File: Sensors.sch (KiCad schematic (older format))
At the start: 42 parts, among them CN4 CONN_HEADER_SMD_4POS_2MM, U10 MPXV4006GP, U11 MPXV4006DP, U12 TLV2333IDR, U16 SFM3020, U17 MPXV4006GP, U7 LPS25HB

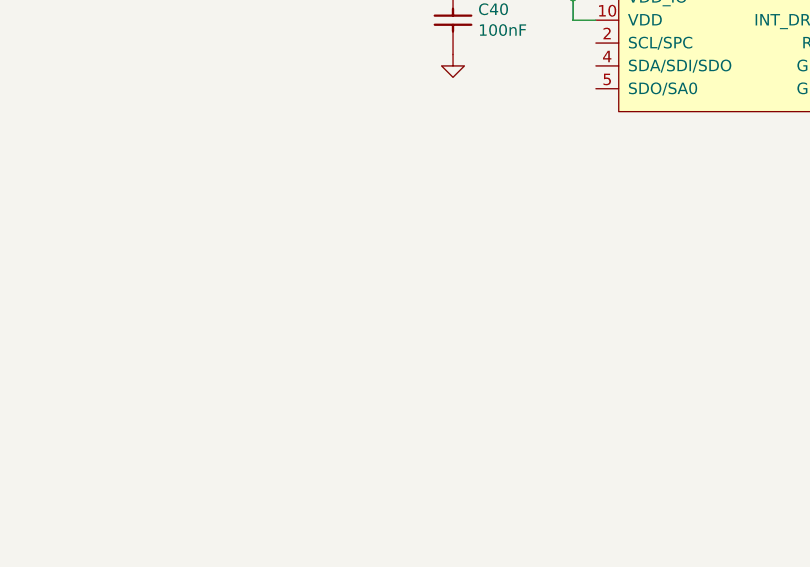
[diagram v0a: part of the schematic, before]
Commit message: MOLEX connector added for SFM3019 external flow sensor
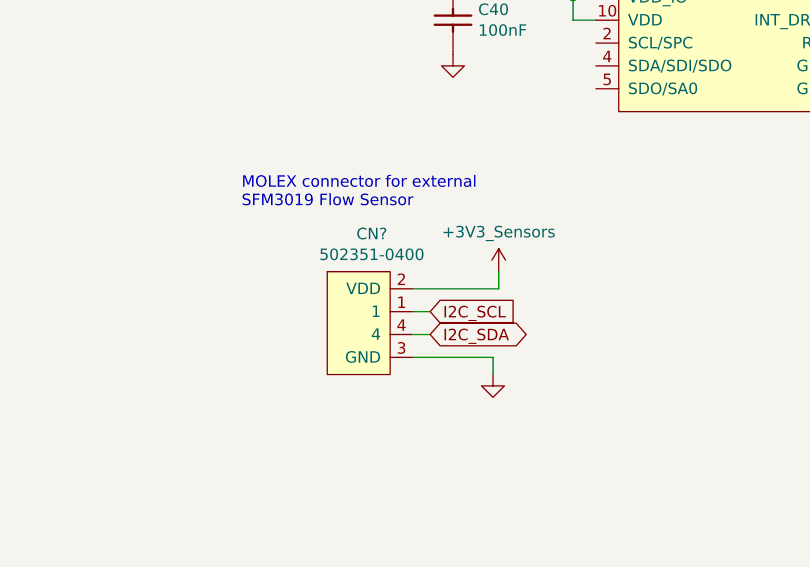
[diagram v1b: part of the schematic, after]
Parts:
- added CN?: 502351-0400, symbol OpenVent:502351-0400
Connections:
- net labels added: +3V3_Sensors, I2C_SCL, I2C_SDA
- wire segments 129 -> 135
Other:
- note added: "MOLEX connector for external\nSFM3019 Flow Sensor"
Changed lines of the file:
@@
 	9625 4775 9625 4675
 Connection ~ 9625 4775
+$Comp
+L OpenVent:502351-0400 CN?
+U 1 1 6027899F
+P 7425 5525
+F 0 "CN?" H 7470 5540 50  0000 C CNN
+F 1 "502351-0400" H 7470 5449 50  0000 C CNN
+F 2 "" H 7425 5525 50  0001 C CNN
+F 3 "" H 7425 5525 50  0001 C CNN
+	1    7425 5525
+	1    0    0    -1
+$EndComp
+$Comp
+L OpenVent:+3V3_Sensors #PWR?
+U 1 1 6027FA4F
+P 8025 5675
+F 0 "#PWR?" H 8025 5525 50  0001 C CNN
+F 1 "+3V3_Sensors" H 8025 5848 50  0000 C CNN
+F 2 "" H 8025 5675 50  0001 C CNN
+F 3 "" H 8025 5675 50  0001 C CNN
+	1    8025 5675
+	1    0    0    -1
+$EndComp
+$Comp
+L OpenVent:GND #PWR?
+U 1 1 6028A518
+P 8000 6125
+F 0 "#PWR?" H 8000 5875 50  0001 C CNN
+F 1 "GND" H 8000 5975 50  0001 C CNN
+F 2 "" H 8000 6125 50  0001 C CNN
+F 3 "" H 8000 6125 50  0001 C CNN
+	1    8000 6125
+	1    0    0    -1
+$EndComp
+Wire Wire Line
+	7650 6050 8000 6050
+Wire Wire Line
+	8000 6050 8000 6125
+Wire Wire Line
+	7650 5750 8025 5750
+Wire Wire Line
+	8025 5750 8025 5675
+Text GLabel 7725 5850 2    50   Input ~ 0
+I2C_SCL
+Text GLabel 7725 5950 2    50   BiDi ~ 0
+I2C_SDA
+Wire Wire Line
+	7650 5850 7725 5850
+Wire Wire Line
+	7650 5950 7725 5950
+Text Notes 6900 5400 0    50   ~ 0
+MOLEX connector for external\nSFM3019 Flow Sensor
 $EndSCHEMATC

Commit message: Removed U16 SFM3020 sensor, changed symbol for CN4 (the off-board connector)
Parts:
- removed C67: 1nF_0603_Ceramic_Capacitor,_10%,_X7R,_25V, symbol OpenVent:1nF_0603_Ceramic_Capacitor,_10%,_X7R,_25V
- removed CN4: CONN_HEADER_SMD_4POS_2MM, symbol OpenVent:CONN_HEADER_SMD_4POS_2MM
- removed R31: 100K_0603_Chip_Resistor,_1%,_0.1W, Resistor_SMD:R_0603_1608Metric, symbol OpenVent:100K_0603_Chip_Resistor,_1%,_0.1W
- removed R34: 200k_0603_Chip_Resistor,_0.1%,_0.1W, Resistor_SMD:R_0603_1608Metric, symbol OpenVent:200k_0603_Chip_Resistor,_0.1%,_0.1W
- removed U16: SFM3020, symbol OpenVent:SFM3020
- added CN4: 502351-0400, symbol OpenVent:502351-0400
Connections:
- net labels removed: SENSIRON-FLOW-SENSOR
- wire segments 135 -> 126
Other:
- note added: "Molex connector for external\nSFM3020 flow sensor"
- note added: "NB Molex connector is into external connector,\nshould same molex connector be used on the PCB,\nor deliberately use a different one so cable can't be\nplugged in wrong way around? LM 08/02/21"
- note removed: "Alternative Flow Sensor Connector"
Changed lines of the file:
@@
 $EndComp
 Text Notes 650  1550 0    60   ~ 0
-Alternative Flow Sensor Connector
+Molex connector for external\nSFM3020 flow sensor
 $Comp
 L OpenVent:GND #GND_031
@@
 	1    0    0    -1
 $EndComp
-NoConn ~ 1600 2150
+NoConn ~ 1475 1950
 Wire Wire Line
 	8550 2575 8550 3075
@@
 	2750 3650 2750 3750
 Wire Wire Line
-	2150 3650 2750 3650
-Wire Wire Line
-	1800 3650 2150 3650
-Wire Wire Line
 	3500 3350 3700 3350
 Wire Wire Line
-	1800 3350 2300 3350
-Wire Wire Line
-	2000 3050 2550 3050
-Wire Wire Line
-	1800 3050 2000 3050
-Wire Wire Line
 	3350 4350 3350 4450
 Wire Wire Line
@@
 Wire Wire Line
 	5800 2050 5700 2050
-Wire Wire Line
-	2300 1850 1600 1850
-Wire Wire Line
-	2300 3350 2300 1850
-Wire Wire Line
-	2150 1950 1600 1950
-Wire Wire Line
-	2150 3650 2150 1950
-Wire Wire Line
-	2000 2050 1600 2050
-Wire Wire Line
-	2000 3050 2000 2050
-Connection ~ 2000 3050
-Connection ~ 2150 3650
-Connection ~ 2300 3350
 Connection ~ 2550 2750
 Connection ~ 2750 4950
@@
 $EndComp
 $Comp
-L OpenVent:CONN_HEADER_SMD_4POS_2MM CN4
-U 1 1 5F8DD0A1
-P 1600 2150
-F 0 "CN4" H 2050 2600 50  0000 L BNN
-F 1 "CONN_HEADER_SMD_4POS_2MM" H 1600 2150 50  0001 C CNN
-F 2 "" H 1600 2150 50  0001 C CNN
-F 3 "" H 1600 2150 50  0001 C CNN
-F 4 "Molex" H 1600 2150 50  0001 C CNN "Mfr"
-F 5 "5600200420" H 1600 2150 50  0001 C CNN "Mfr_PN"
-	1    1600 2150
-	-1   0    0    -1
-$EndComp
-$Comp
 L OpenVent:10nF_0603_Ceramic_Capacitor,_10%,_50V,_X7R- C32
 U 1 1 5F8DD0A0
@@
 Wire Wire Line
 	1800 4650 2950 4650
-Wire Wire Line
-	2300 3350 2950 3350
 $Comp
 L OpenVent:TLV2333IDR U12
@@
 Connection ~ 2750 5750
 $Comp
-L OpenVent:+5V #5V_010
-U 1 1 5FFC79F0
-P 1250 7000
-F 0 "#5V_010" H 1250 7000 20  0001 C CNN
-F 1 "+5V" H 1250 7150 50  0000 C CNN
-F 2 "" H 1250 7000 70  0000 C CNN
-F 3 "" H 1250 7000 70  0000 C CNN
-	1    1250 7000
-	1    0    0    -1
-$EndComp
-Wire Wire Line
-	1250 7125 1250 7000
-$Comp
-L OpenVent:GND #GND_030
-U 1 1 5FFDC913
-P 1250 7375
-F 0 "#GND_030" H 1250 7375 20  0001 C CNN
-F 1 "GND" H 1250 7305 50  0001 C CNN
-F 2 "" H 1250 7375 70  0000 C CNN
-F 3 "" H 1250 7375 70  0000 C CNN
-	1    1250 7375
-	1    0    0    -1
-$EndComp
-Wire Wire Line
-	1250 7375 1250 7225
-Text GLabel 4475 7125 2    60   Output ~ 0
-SENSIRON-FLOW-SENSOR
-$Comp
-L OpenVent:1nF_0603_Ceramic_Capacitor,_10%,_X7R,_25V C67
-U 1 1 5FFEE081
-P 3050 7250
-F 0 "C67" V 3054 7260 50  0000 L CNN
-F 1 "1nF_0603_Ceramic_Capacitor,_10%,_X7R,_25V" H 2525 7475 50  0001 C CNN
-F 2 "" H 3050 7250 50  0001 C CNN
-F 3 "" H 3050 7250 50  0001 C CNN
-F 4 "1nF" V 3145 7260 50  0000 L CNN "Val"
-F 5 "25V" H 2825 6925 50  0001 C CNN "Voltage"
-F 6 "10%" H 3125 6850 50  0001 C CNN "Tolerance"
-	1    3050 7250
-	0    1    1    0
-$EndComp
-$Comp
-L OpenVent:200k_0603_Chip_Resistor,_0.1%,_0.1W R34
-U 1 1 5FFF309C
-P 4150 7500
-F 0 "R34" V 4300 7150 50  0000 L BNN
-F 1 "200k_0603_Chip_Resistor,_0.1%,_0.1W" V 4150 7350 50  0001 C CNN
-F 2 "Resistor_SMD:R_0603_1608Metric" H 4050 7360 50  0001 C CNN
-F 3 "" H 4050 7360 50  0001 C CNN
-F 4 "0.1%" V 4100 7200 50  0000 C CNN "Tolerance"
-F 5 "200k" V 4200 7200 50  0000 C CNN "Val"
-F 6 "0.1W" H 4150 7500 50  0001 C CNN "Watt"
-	1    4150 7500
-	0    -1   -1   0
-$EndComp
-$Comp
-L OpenVent:100K_0603_Chip_Resistor,_1%,_0.1W R31
-U 1 1 5FFF367C
-P 3800 7025
-F 0 "R31" H 3800 6975 50  0000 L BNN
-F 1 "100K_0603_Chip_Resistor,_1%,_0.1W" H 3800 6775 50  0001 C CNN
-F 2 "Resistor_SMD:R_0603_1608Metric" H 3800 6685 50  0001 C CNN
-F 3 "" H 3800 6685 50  0001 C CNN
-F 4 "1%" V 1400 -475 50  0001 C CNN "Tolerance"
-F 5 "100k" H 3900 6825 50  0000 C CNN "Val"
-F 6 "0.1W" H 3800 7025 50  0001 C CNN "Watt"
-	1    3800 7025
-	1    0    0    -1
-$EndComp
-$Comp
-L OpenVent:GND #GND_045
-U 1 1 5FFF4998
-P 2950 7575
-F 0 "#GND_045" H 2950 7575 20  0001 C CNN
-F 1 "GND" H 2950 7505 50  0001 C CNN
-F 2 "" H 2950 7575 70  0000 C CNN
-F 3 "" H 2950 7575 70  0000 C CNN
-	1    2950 7575
-	1    0    0    -1
-$EndComp
-Wire Wire Line
-	2950 7575 2950 7450
-Wire Wire Line
-	2950 7125 2950 7150
-Wire Wire Line
-	2950 7125 3700 7125
-$Comp
-L OpenVent:GND #GND_047
-U 1 1 60007151
-P 4250 7600
-F 0 "#GND_047" H 4250 7600 20  0001 C CNN
-F 1 "GND" H 4250 7530 50  0001 C CNN
-F 2 "" H 4250 7600 70  0000 C CNN
-F 3 "" H 4250 7600 70  0000 C CNN
-	1    4250 7600
-	1    0    0    -1
-$EndComp
-Wire Wire Line
-	4250 7200 4250 7125
-Wire Wire Line
-	4250 7125 4100 7125
-Wire Wire Line
-	4250 7125 4475 7125
-Connection ~ 4250 7125
-$Comp
-L OpenVent:SFM3020 U16
-U 1 1 5FFDAFCB
-P 1350 7125
-F 0 "U16" H 1610 7360 50  0000 C CNN
-F 1 "SFM3020" H 1610 7269 50  0000 C CNN
-F 2 "" H 1350 7125 50  0001 C CNN
-F 3 "" H 1350 7125 50  0001 C CNN
-	1    1350 7125
-	1    0    0    -1
-$EndComp
-Wire Wire Line
-	1970 7125 2950 7125
-Connection ~ 2950 7125
-$Comp
 L OpenVent:LPS25HB U7
 U 1 1 5FFAE568
@@
 Text Notes 6900 5400 0    50   ~ 0
 MOLEX connector for external\nSFM3019 Flow Sensor
+$Comp
+L OpenVent:502351-0400 CN4
+U 1 1 602C9734
+P 1250 1625
+F 0 "CN4" H 1295 1640 50  0000 C CNN
+F 1 "502351-0400" H 1295 1549 50  0000 C CNN
+F 2 "" H 1250 1625 50  0001 C CNN
+F 3 "" H 1250 1625 50  0001 C CNN
+	1    1250 1625
+	1    0    0    -1
+$EndComp
+Wire Wire Line
+	1800 3650 1875 3650
+Wire Wire Line
+	1800 3050 2325 3050
+Wire Wire Line
+	1800 3350 2075 3350
+Wire Wire Line
+	2325 3050 2325 1850
+Wire Wire Line
+	2325 1850 1475 1850
+Connection ~ 2325 3050
+Wire Wire Line
+	2325 3050 2550 3050
+Wire Wire Line
+	2075 3350 2075 2050
+Wire Wire Line
+	2075 2050 1475 2050
+Connection ~ 2075 3350
+Wire Wire Line
+	2075 3350 2950 3350
+Wire Wire Line
+	1475 2150 1875 2150
+Wire Wire Line
+	1875 2150 1875 3650
+Connection ~ 1875 3650
+Wire Wire Line
+	1875 3650 2750 3650
+Text Notes 625  1150 0    60   ~ 0
+NB Molex connector is into external connector,\nshould same molex connector be used on the PCB,\nor deliberately use a different one so cable can't be\nplugged in wrong way around? LM 08/02/21
 $EndSCHEMATC

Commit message: More fixing up of the FPGA symbols, lashed up the sigma delta A/D converter circuitry.  Fixed up the LCD page.  Two displays, two separate enables needed here folks.  FPGA I/O banks power supplies' needs another looking at.  Still lots of stuff to clean up here...
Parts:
- gave numbers to parts that had none: 1
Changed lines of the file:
@@
 Connection ~ 9625 4775
 $Comp
-L OpenVent:502351-0400 CN?
+L OpenVent:502351-0400 CN3
 U 1 1 6027899F
 P 7425 5525
-F 0 "CN?" H 7470 5540 50  0000 C CNN
+F 0 "CN3" H 7470 5540 50  0000 C CNN
 F 1 "502351-0400" H 7470 5449 50  0000 C CNN
 F 2 "" H 7425 5525 50  0001 C CNN
@@
 $EndComp
 $Comp
-L OpenVent:+3V3_Sensors #PWR?
+L OpenVent:+3V3_Sensors #PWR03
 U 1 1 6027FA4F
 P 8025 5675
-F 0 "#PWR?" H 8025 5525 50  0001 C CNN
+F 0 "#PWR03" H 8025 5525 50  0001 C CNN
 F 1 "+3V3_Sensors" H 8025 5848 50  0000 C CNN
 F 2 "" H 8025 5675 50  0001 C CNN
@@
 $EndComp
 $Comp
-L OpenVent:GND #PWR?
+L OpenVent:GND #PWR01
 U 1 1 6028A518
 P 8000 6125
-F 0 "#PWR?" H 8000 5875 50  0001 C CNN
+F 0 "#PWR01" H 8000 5875 50  0001 C CNN
 F 1 "GND" H 8000 5975 50  0001 C CNN
 F 2 "" H 8000 6125 50  0001 C CNN

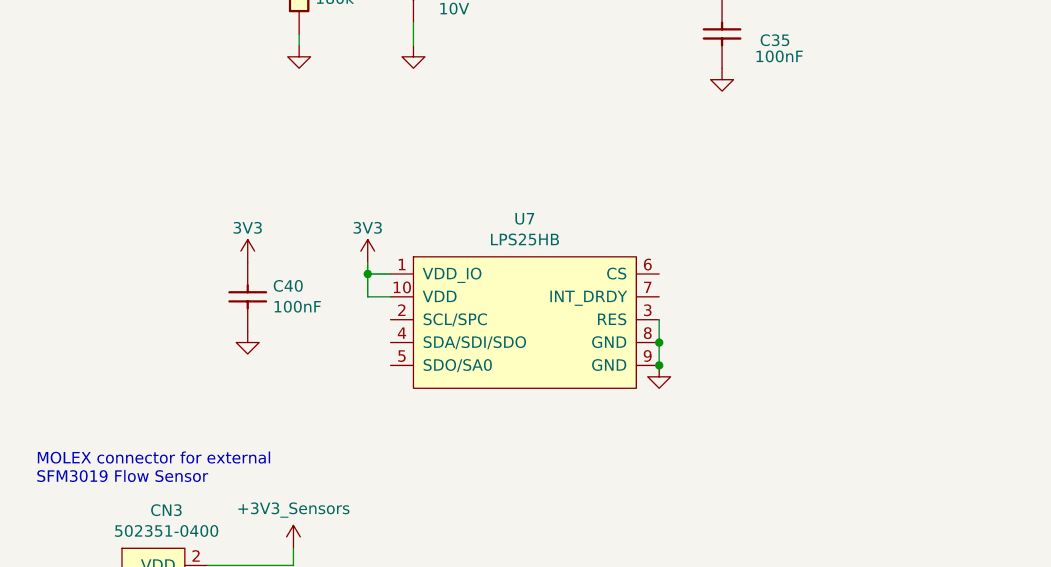
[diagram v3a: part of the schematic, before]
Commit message: Added SPI between FPGA, MCU, sensor
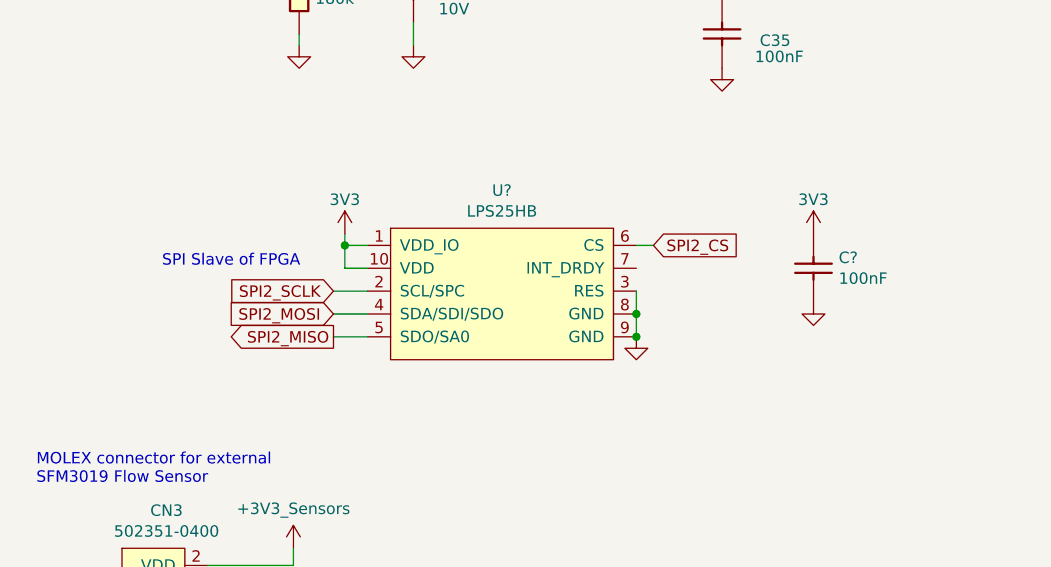
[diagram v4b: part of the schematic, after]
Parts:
- removed C40: 100nF_0603_Ceramic_Capacitor,_10%,_X7R,_25V, symbol OpenVent:100nF_0603_Ceramic_Capacitor,_10%,_X7R,_25V
- removed U7: LPS25HB, symbol OpenVent:LPS25HB
- added C?: 100nF_0603_Ceramic_Capacitor,_10%,_X7R,_25V, symbol OpenVent:100nF_0603_Ceramic_Capacitor,_10%,_X7R,_25V
- added U?: LPS25HB, symbol OpenVent:LPS25HB
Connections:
- net +3V3: now also C?.1, U?.1 (VDD_IO), U?.10 (VDD)
- net GND: now also C?.2, U?.3 (RES), U?.8 (GND), U?.9 (GND)
- new net SPI2_CS: U?.6 (CS)
- new net SPI2_MISO: U?.5 (SDO/SA0)
- new net SPI2_MOSI: U?.4 (SDA/SDI/SDO)
- new net SPI2_SCLK: U?.2 (SCL/SPC)
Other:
- note added: "SPI Slave of FPGA"
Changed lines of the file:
@@
 Connection ~ 2750 5750
-$Comp
-L OpenVent:LPS25HB U7
-U 1 1 5FFAE568
-P 8550 4475
-F 0 "U7" H 9037 4715 50  0000 C CNN
-F 1 "LPS25HB" H 9037 4624 50  0000 C CNN
-F 2 "" H 8550 4475 50  0001 C CNN
-F 3 "" H 8550 4475 50  0001 C CNN
-	1    8550 4475
-	1    0    0    -1
-$EndComp
-$Comp
-L OpenVent:3V3 #3V3_?
-U 1 1 5FFCC9B7
-P 8350 4425
-AR Path="/5F988182/5FFCC9B7" Ref="#3V3_?"  Part="1"
-AR Path="/5F8F3873/5FFCC9B7" Ref="#3V3_08"  Part="1"
-F 0 "#3V3_08" H 8350 4425 20  0001 C CNN
-F 1 "3V3" H 8350 4575 50  0000 C CNN
-F 2 "" H 8350 4425 70  0001 C CNN
-F 3 "" H 8350 4425 70  0001 C CNN
-	1    8350 4425
-	1    0    0    -1
-$EndComp
-Wire Wire Line
-	8450 4475 8350 4475
-Wire Wire Line
-	8350 4475 8350 4425
-Wire Wire Line
-	8450 4575 8350 4575
-Wire Wire Line
-	8350 4575 8350 4475
-Connection ~ 8350 4475
-$Comp
-L OpenVent:3V3 #3V3_?
-U 1 1 5FFDC823
-P 7825 4425
-AR Path="/5F988182/5FFDC823" Ref="#3V3_?"  Part="1"
-AR Path="/5F8F3873/5FFDC823" Ref="#3V3_07"  Part="1"
-F 0 "#3V3_07" H 7825 4425 20  0001 C CNN
-F 1 "3V3" H 7825 4575 50  0000 C CNN
-F 2 "" H 7825 4425 70  0001 C CNN
-F 3 "" H 7825 4425 70  0001 C CNN
-	1    7825 4425
-	1    0    0    -1
-$EndComp
-$Comp
-L OpenVent:100nF_0603_Ceramic_Capacitor,_10%,_X7R,_25V C40
-U 1 1 5FFDE287
-P 7925 4525
-F 0 "C40" V 7929 4535 50  0000 L CNN
-F 1 "100nF_0603_Ceramic_Capacitor,_10%,_X7R,_25V" H 7925 4525 50  0001 C CNN
-F 2 "" H 7925 4525 50  0001 C CNN
-F 3 "" H 7925 4525 50  0001 C CNN
-F 4 "100nF" V 8020 4535 50  0000 L CNN "Val"
-F 5 "25V" H 7925 4525 50  0001 C CNN "Voltage"
-F 6 "10%" H 7925 4525 50  0001 C CNN "Tolerance"
-	1    7925 4525
-	0    1    1    0
-$EndComp
-$Comp
-L OpenVent:GND #GND_03
-U 1 1 5FFDE6DE
-P 7825 4725
-F 0 "#GND_03" H 7825 4725 20  0001 C CNN
-F 1 "GND" H 7825 4655 50  0001 C CNN
-F 2 "" H 7825 4725 70  0000 C CNN
-F 3 "" H 7825 4725 70  0000 C CNN
-	1    7825 4725
-	1    0    0    -1
-$EndComp
-$Comp
-L OpenVent:GND #GND_04
-U 1 1 5FFE65C3
-P 9625 4875
-F 0 "#GND_04" H 9625 4875 20  0001 C CNN
-F 1 "GND" H 9625 4805 50  0001 C CNN
-F 2 "" H 9625 4875 70  0000 C CNN
-F 3 "" H 9625 4875 70  0000 C CNN
-	1    9625 4875
-	1    0    0    -1
-$EndComp
-Wire Wire Line
-	9625 4875 9625 4775
-Connection ~ 9625 4875
-Wire Wire Line
-	9625 4775 9625 4675
-Connection ~ 9625 4775
 $Comp
 L OpenVent:502351-0400 CN3
@@
 Text Notes 625  1150 0    60   ~ 0
 NB Molex connector is into external connector,\nshould same molex connector be used on the PCB,\nor deliberately use a different one so cable can't be\nplugged in wrong way around? LM 08/02/21
+$Comp
+L OpenVent:LPS25HB U?
+U 1 1 602FA2A4
+P 8450 4350
+F 0 "U?" H 8937 4590 50  0000 C CNN
+F 1 "LPS25HB" H 8937 4499 50  0000 C CNN
+F 2 "" H 8450 4350 50  0001 C CNN
+F 3 "" H 8450 4350 50  0001 C CNN
+	1    8450 4350
+	1    0    0    -1
+$EndComp
+$Comp
+L OpenVent:3V3 #3V3_?
+U 1 1 602FA2AA
+P 8250 4300
+AR Path="/5F988182/602FA2AA" Ref="#3V3_?"  Part="1"
+AR Path="/5F8F3873/602FA2AA" Ref="#3V3_?"  Part="1"
+F 0 "#3V3_?" H 8250 4300 20  0001 C CNN
+F 1 "3V3" H 8250 4450 50  0000 C CNN
+F 2 "" H 8250 4300 70  0001 C CNN
+F 3 "" H 8250 4300 70  0001 C CNN
+	1    8250 4300
+	1    0    0    -1
+$EndComp
+Wire Wire Line
+	8350 4350 8250 4350
+Wire Wire Line
+	8350 4450 8250 4450
+$Comp
+L OpenVent:3V3 #3V3_?
+U 1 1 602FA2B5
+P 10300 4300
+AR Path="/5F988182/602FA2B5" Ref="#3V3_?"  Part="1"
+AR Path="/5F8F3873/602FA2B5" Ref="#3V3_?"  Part="1"
+F 0 "#3V3_?" H 10300 4300 20  0001 C CNN
+F 1 "3V3" H 10300 4450 50  0000 C CNN
+F 2 "" H 10300 4300 70  0001 C CNN
+F 3 "" H 10300 4300 70  0001 C CNN
+	1    10300 4300
+	1    0    0    -1
+$EndComp
+$Comp
+L OpenVent:100nF_0603_Ceramic_Capacitor,_10%,_X7R,_25V C?
+U 1 1 602FA2BE
+P 10400 4400
+F 0 "C?" V 10404 4410 50  0000 L CNN
+F 1 "100nF_0603_Ceramic_Capacitor,_10%,_X7R,_25V" H 10400 4400 50  0001 C CNN
+F 2 "" H 10400 4400 50  0001 C CNN
+F 3 "" H 10400 4400 50  0001 C CNN
+F 4 "100nF" V 10495 4410 50  0000 L CNN "Val"
+F 5 "25V" H 10400 4400 50  0001 C CNN "Voltage"
+F 6 "10%" H 10400 4400 50  0001 C CNN "Tolerance"
+	1    10400 4400
+	0    1    1    0
+$EndComp
+$Comp
+L OpenVent:GND #GND_?
+U 1 1 602FA2C4
+P 10300 4600
+F 0 "#GND_?" H 10300 4600 20  0001 C CNN
+F 1 "GND" H 10300 4530 50  0001 C CNN
+F 2 "" H 10300 4600 70  0000 C CNN
+F 3 "" H 10300 4600 70  0000 C CNN
+	1    10300 4600
+	1    0    0    -1
+$EndComp
+$Comp
+L OpenVent:GND #GND_?
+U 1 1 602FA2CA
+P 9525 4750
+F 0 "#GND_?" H 9525 4750 20  0001 C CNN
+F 1 "GND" H 9525 4680 50  0001 C CNN
+F 2 "" H 9525 4750 70  0000 C CNN
+F 3 "" H 9525 4750 70  0000 C CNN
+	1    9525 4750
+	1    0    0    -1
+$EndComp
+Wire Wire Line
+	9525 4750 9525 4650
+Connection ~ 9525 4750
+Wire Wire Line
+	9525 4650 9525 4550
+Connection ~ 9525 4650
+Text GLabel 9600 4350 2    50   Input ~ 0
+SPI2_CS
+Text GLabel 8200 4750 0    50   Output ~ 0
+SPI2_MISO
+Text GLabel 8200 4650 0    50   Input ~ 0
+SPI2_MOSI
+Text GLabel 8200 4550 0    50   Input ~ 0
+SPI2_SCLK
+Wire Wire Line
+	8250 4300 8250 4350
+Wire Wire Line
+	8350 4750 8200 4750
+Wire Wire Line
+	8350 4650 8200 4650
+Wire Wire Line
+	8350 4550 8200 4550
+Connection ~ 8250 4350
+Wire Wire Line
+	8250 4350 8250 4450
+Wire Wire Line
+	9525 4350 9600 4350
+Text Notes 7450 4450 0    50   ~ 0
+SPI Slave of FPGA
 $EndSCHEMATC
